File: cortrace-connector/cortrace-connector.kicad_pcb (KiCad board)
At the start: 2 copper layers, 34.5 x 22 mm, 8 parts, among them J1 FPGA-PORT, J2 Conn_ARM_Cortex_Debug_ETM_20, J4 SWD-PORT

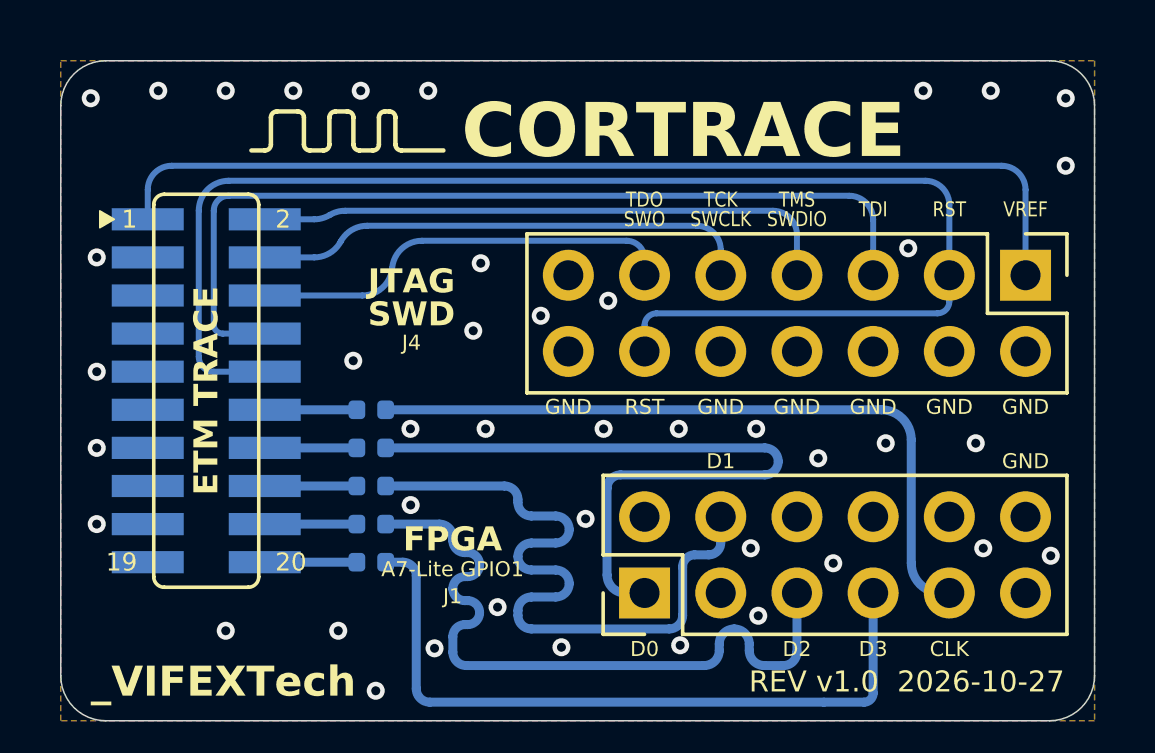
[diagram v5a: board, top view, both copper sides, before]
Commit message: feat(connector): use a 1.27 mm SMD female socket for the TRACE port
Swap J2 from the pin header footprint to the stock KiCad PinSocket_2x10_P1.27mm_Vertical_SMD. Its pads are already numbered mirrored, so the back-side placement needs no pad swap and the footprint matches the library again.
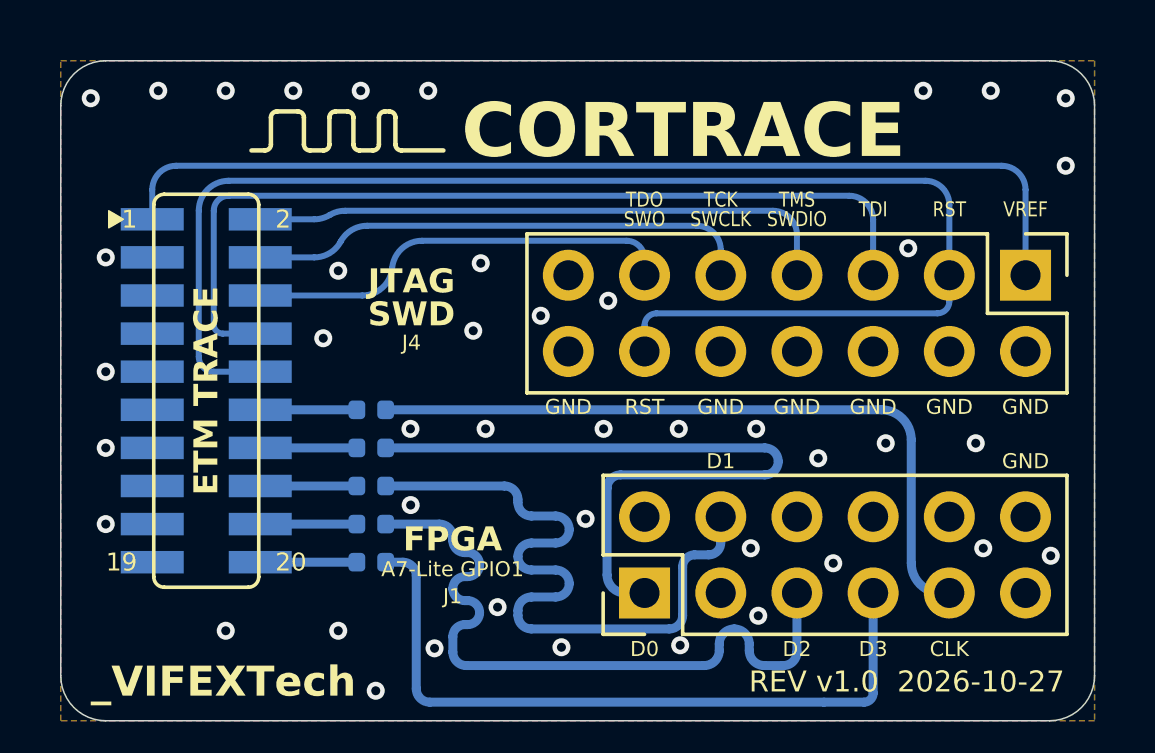
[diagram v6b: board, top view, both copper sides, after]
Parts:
- J2: footprint Connector_PinHeader_1.27mm:PinHeader_2x10_P1.27mm_Vertical_SMD -> Connector_PinSocket_1.27mm:PinSocket_2x10_P1.27mm_Vertical_SMD
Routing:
- net GND: vias 42 -> 43
